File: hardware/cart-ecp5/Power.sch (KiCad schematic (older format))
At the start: 31 parts

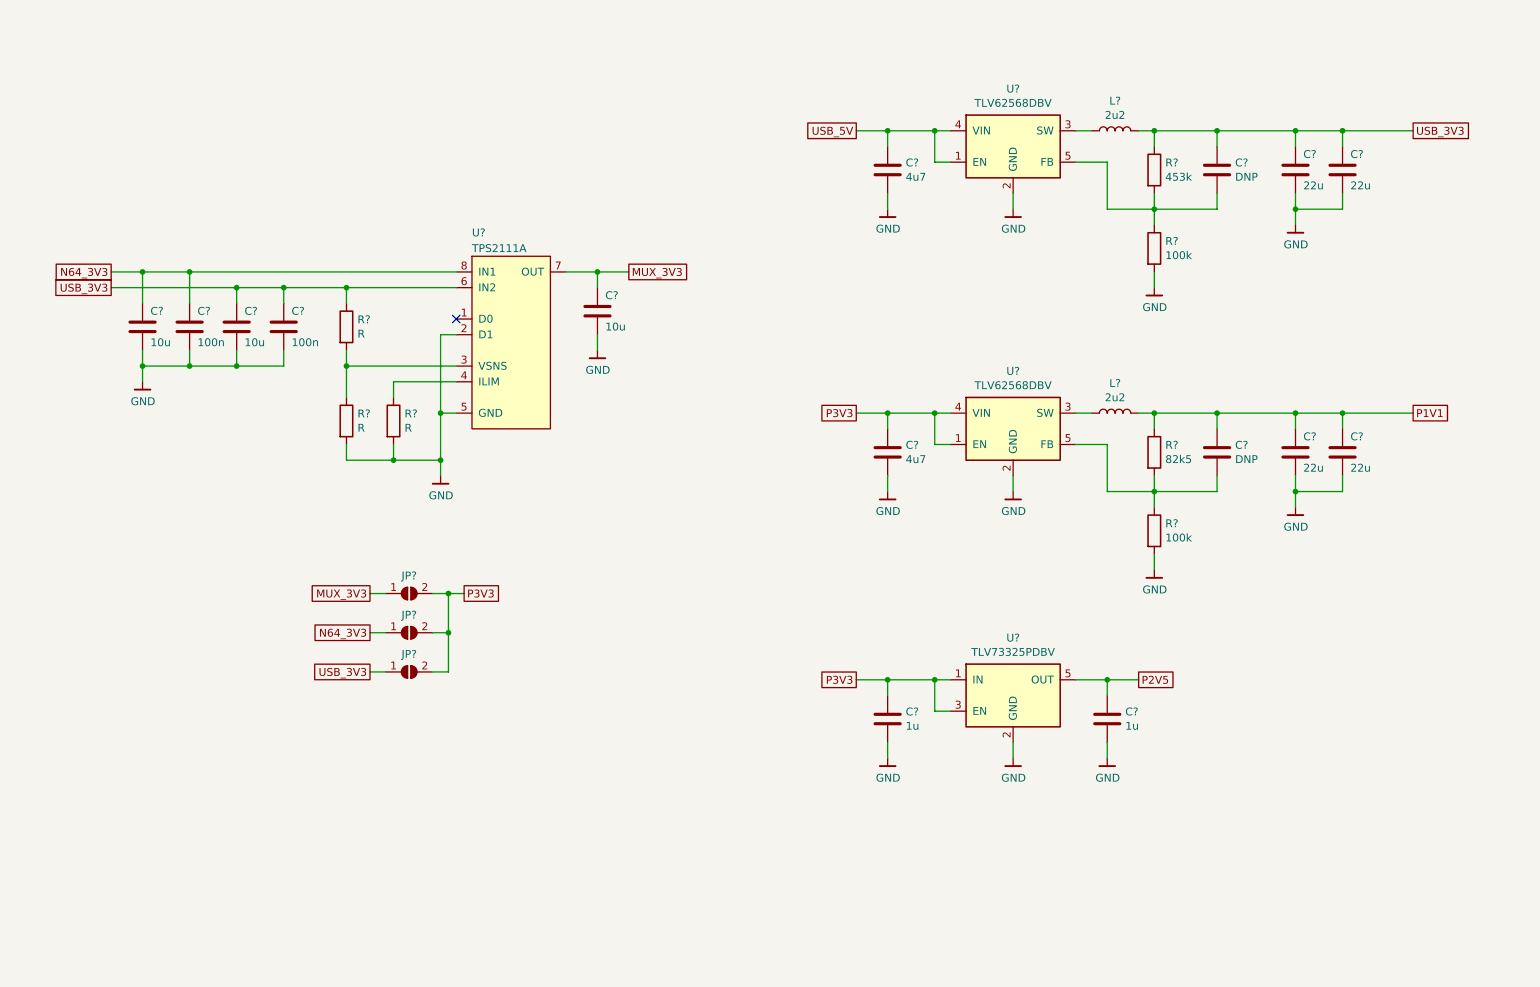
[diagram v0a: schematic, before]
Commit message: First pass annotation and footprint assignment complete
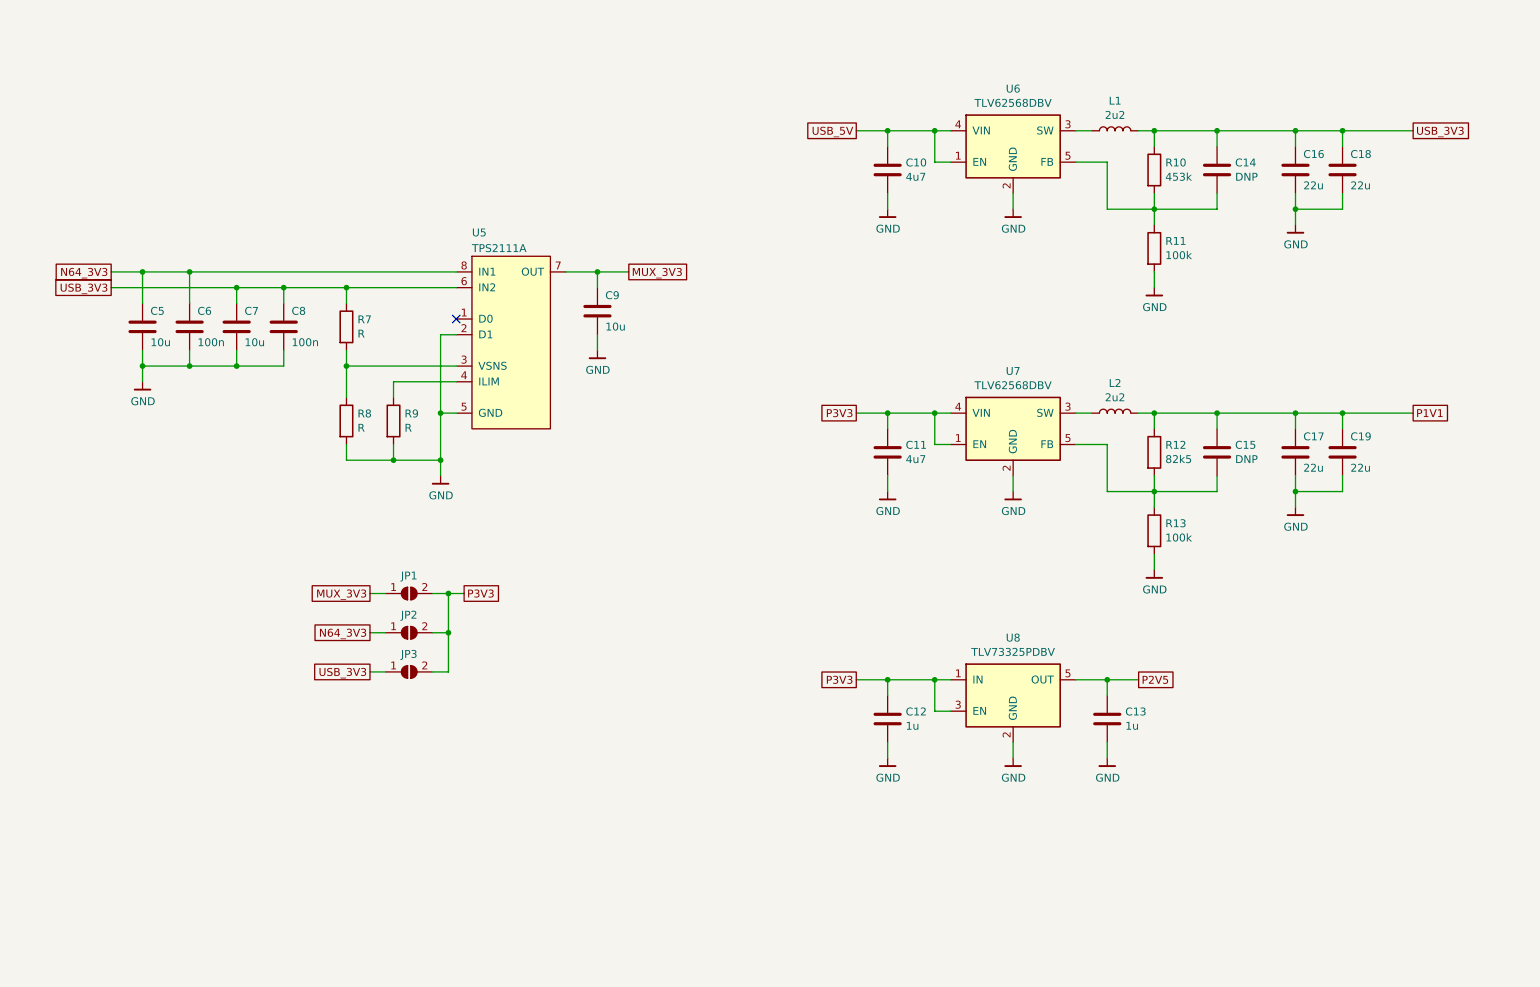
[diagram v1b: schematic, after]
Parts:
- C10, C11, C12, C13, C14, C15, C16, C17, C18, C19: renamed from C?; footprint (none) -> Capacitor_SMD:C_0603_1608Metric
- L1, L2: renamed from L?; footprint (none) -> Inductor_SMD:L_Taiyo-Yuden_NR-40xx
- R10, R11, R12, R13: renamed from R?; footprint (none) -> Resistor_SMD:R_0603_1608Metric
- gave numbers to parts that had none: 10

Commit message: Fixes for footprint assignment
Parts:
- C16, C17, C18, C19: footprint Capacitor_SMD:C_0603_1608Metric -> Capacitor_SMD:C_0805_2012Metric
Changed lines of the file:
@@
 F 0 "C18" H 9550 2150 50  0000 L CNN
 F 1 "22u" H 9550 1950 50  0000 L CNN
-F 2 "Capacitor_SMD:C_0603_1608Metric" H 9538 1900 50  0001 C CNN
+F 2 "Capacitor_SMD:C_0805_2012Metric" H 9538 1900 50  0001 C CNN
 F 3 "~" H 9500 2050 50  0001 C CNN
 	1    9500 2050
@@
 F 0 "C16" H 9250 2150 50  0000 L CNN
 F 1 "22u" H 9250 1950 50  0000 L CNN
-F 2 "Capacitor_SMD:C_0603_1608Metric" H 9238 1900 50  0001 C CNN
+F 2 "Capacitor_SMD:C_0805_2012Metric" H 9238 1900 50  0001 C CNN
 F 3 "~" H 9200 2050 50  0001 C CNN
 	1    9200 2050
@@
 F 0 "C19" H 9550 3950 50  0000 L CNN
 F 1 "22u" H 9550 3750 50  0000 L CNN
-F 2 "Capacitor_SMD:C_0603_1608Metric" H 9538 3700 50  0001 C CNN
+F 2 "Capacitor_SMD:C_0805_2012Metric" H 9538 3700 50  0001 C CNN
 F 3 "~" H 9500 3850 50  0001 C CNN
 	1    9500 3850
@@
 F 0 "C17" H 9250 3950 50  0000 L CNN
 F 1 "22u" H 9250 3750 50  0000 L CNN
-F 2 "Capacitor_SMD:C_0603_1608Metric" H 9238 3700 50  0001 C CNN
+F 2 "Capacitor_SMD:C_0805_2012Metric" H 9238 3700 50  0001 C CNN
 F 3 "~" H 9200 3850 50  0001 C CNN
 	1    9200 3850

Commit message: Assign FPGA pins for N64 cartridge bus
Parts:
- C14, C15, C52, C53: footprint Capacitor_SMD:C_0603_1608Metric -> Capacitor_SMD:C_0402_1005Metric
- C51: footprint Capacitor_SMD:C_0805_2012Metric -> Capacitor_SMD:C_0603_1608Metric
- R10, R11, R12, R13, R7, R8, R9: footprint Resistor_SMD:R_0603_1608Metric -> Resistor_SMD:R_0402_1005Metric
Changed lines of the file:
@@
 F 0 "R9" H 3520 3696 50  0000 L CNN
 F 1 "R" H 3520 3605 50  0000 L CNN
-F 2 "Resistor_SMD:R_0603_1608Metric" V 3380 3650 50  0001 C CNN
+F 2 "Resistor_SMD:R_0402_1005Metric" V 3380 3650 50  0001 C CNN
 F 3 "~" H 3450 3650 50  0001 C CNN
 	1    3450 3650
@@
 F 0 "R8" H 3220 3696 50  0000 L CNN
 F 1 "R" H 3220 3605 50  0000 L CNN
-F 2 "Resistor_SMD:R_0603_1608Metric" V 3080 3650 50  0001 C CNN
+F 2 "Resistor_SMD:R_0402_1005Metric" V 3080 3650 50  0001 C CNN
 F 3 "~" H 3150 3650 50  0001 C CNN
 	1    3150 3650
@@
 F 0 "R7" H 3220 3096 50  0000 L CNN
 F 1 "R" H 3220 3005 50  0000 L CNN
-F 2 "Resistor_SMD:R_0603_1608Metric" V 3080 3050 50  0001 C CNN
+F 2 "Resistor_SMD:R_0402_1005Metric" V 3080 3050 50  0001 C CNN
 F 3 "~" H 3150 3050 50  0001 C CNN
 	1    3150 3050
@@
 F 0 "C8" H 2800 3150 50  0000 L CNN
 F 1 "100n" H 2800 2950 50  0000 L CNN
-F 2 "Capacitor_SMD:C_0603_1608Metric" H 2788 2900 50  0001 C CNN
+F 2 "Capacitor_SMD:C_0402_1005Metric" H 2788 2900 50  0001 C CNN
 F 3 "~" H 2750 3050 50  0001 C CNN
 F 4 "" H 2750 3050 50  0001 C CNN "MPN"
@@
 F 0 "C6" H 2200 3150 50  0000 L CNN
 F 1 "100n" H 2200 2950 50  0000 L CNN
-F 2 "Capacitor_SMD:C_0603_1608Metric" H 2188 2900 50  0001 C CNN
+F 2 "Capacitor_SMD:C_0402_1005Metric" H 2188 2900 50  0001 C CNN
 F 3 "~" H 2150 3050 50  0001 C CNN
 F 4 "" H 2150 3050 50  0001 C CNN "MPN"
@@
 F 0 "C9" H 4800 3050 50  0000 L CNN
 F 1 "10u" H 4800 2850 50  0000 L CNN
-F 2 "Capacitor_SMD:C_0805_2012Metric" H 4788 2800 50  0001 C CNN
+F 2 "Capacitor_SMD:C_0603_1608Metric" H 4788 2800 50  0001 C CNN
 F 3 "~" H 4750 2950 50  0001 C CNN
 F 4 "" H 4750 2950 50  0001 C CNN "MPN"
@@
 F 0 "C14" H 8815 2096 50  0000 L CNN
 F 1 "DNP" H 8815 2005 50  0000 L CNN
-F 2 "Capacitor_SMD:C_0603_1608Metric" H 8738 1900 50  0001 C CNN
+F 2 "Capacitor_SMD:C_0402_1005Metric" H 8738 1900 50  0001 C CNN
 F 3 "~" H 8700 2050 50  0001 C CNN
 	1    8700 2050
@@
 F 0 "R10" H 8370 2096 50  0000 L CNN
 F 1 "453k" H 8370 2005 50  0000 L CNN
-F 2 "Resistor_SMD:R_0603_1608Metric" V 8230 2050 50  0001 C CNN
+F 2 "Resistor_SMD:R_0402_1005Metric" V 8230 2050 50  0001 C CNN
 F 3 "~" H 8300 2050 50  0001 C CNN
 	1    8300 2050
@@
 F 0 "R11" H 8370 2596 50  0000 L CNN
 F 1 "100k" H 8370 2505 50  0000 L CNN
-F 2 "Resistor_SMD:R_0603_1608Metric" V 8230 2550 50  0001 C CNN
+F 2 "Resistor_SMD:R_0402_1005Metric" V 8230 2550 50  0001 C CNN
 F 3 "~" H 8300 2550 50  0001 C CNN
 	1    8300 2550
@@
 F 0 "C15" H 8815 3896 50  0000 L CNN
 F 1 "DNP" H 8815 3805 50  0000 L CNN
-F 2 "Capacitor_SMD:C_0603_1608Metric" H 8738 3700 50  0001 C CNN
+F 2 "Capacitor_SMD:C_0402_1005Metric" H 8738 3700 50  0001 C CNN
 F 3 "~" H 8700 3850 50  0001 C CNN
 	1    8700 3850
@@
 F 0 "R12" H 8370 3896 50  0000 L CNN
 F 1 "82k5" H 8370 3805 50  0000 L CNN
-F 2 "Resistor_SMD:R_0603_1608Metric" V 8230 3850 50  0001 C CNN
+F 2 "Resistor_SMD:R_0402_1005Metric" V 8230 3850 50  0001 C CNN
 F 3 "~" H 8300 3850 50  0001 C CNN
 	1    8300 3850
@@
 F 0 "R13" H 8370 4396 50  0000 L CNN
 F 1 "100k" H 8370 4305 50  0000 L CNN
-F 2 "Resistor_SMD:R_0603_1608Metric" V 8230 4350 50  0001 C CNN
+F 2 "Resistor_SMD:R_0402_1005Metric" V 8230 4350 50  0001 C CNN
 F 3 "~" H 8300 4350 50  0001 C CNN
 	1    8300 4350

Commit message: Use 0805 power inductors
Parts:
- L1, L2: footprint Inductor_SMD:L_Taiyo-Yuden_NR-40xx -> Inductor_SMD:L_0805_2012Metric
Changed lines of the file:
@@
 F 0 "L1" V 8240 1800 50  0000 C CNN
 F 1 "2u2" V 8149 1800 50  0000 C CNN
-F 2 "Inductor_SMD:L_Taiyo-Yuden_NR-40xx" H 8050 1800 50  0001 C CNN
+F 2 "Inductor_SMD:L_0805_2012Metric" H 8050 1800 50  0001 C CNN
 F 3 "~" H 8050 1800 50  0001 C CNN
 	1    8050 1800
@@
 F 0 "L2" V 8240 3600 50  0000 C CNN
 F 1 "2u2" V 8149 3600 50  0000 C CNN
-F 2 "Inductor_SMD:L_Taiyo-Yuden_NR-40xx" H 8050 3600 50  0001 C CNN
+F 2 "Inductor_SMD:L_0805_2012Metric" H 8050 3600 50  0001 C CNN
 F 3 "~" H 8050 3600 50  0001 C CNN
 	1    8050 3600

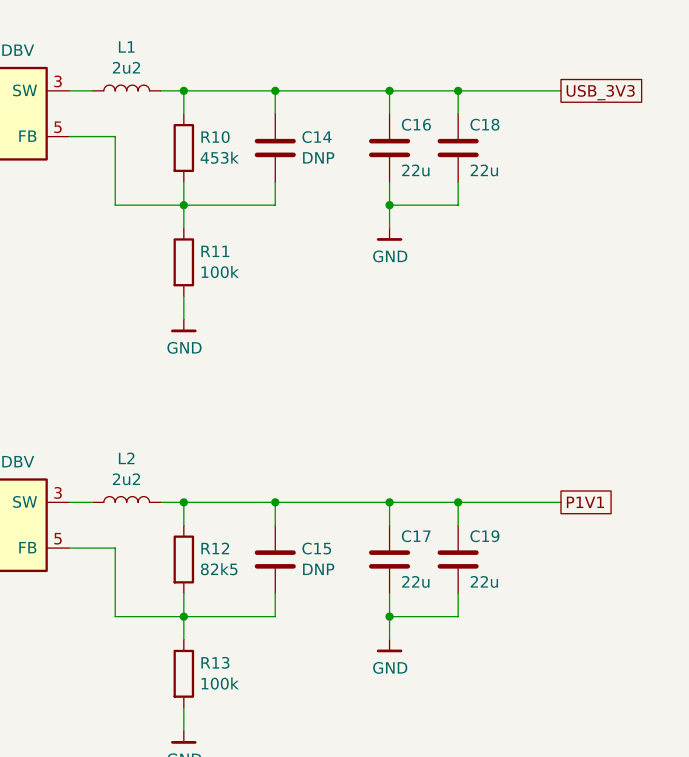
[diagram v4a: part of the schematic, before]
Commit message: Reduce the area of the voltage regulators
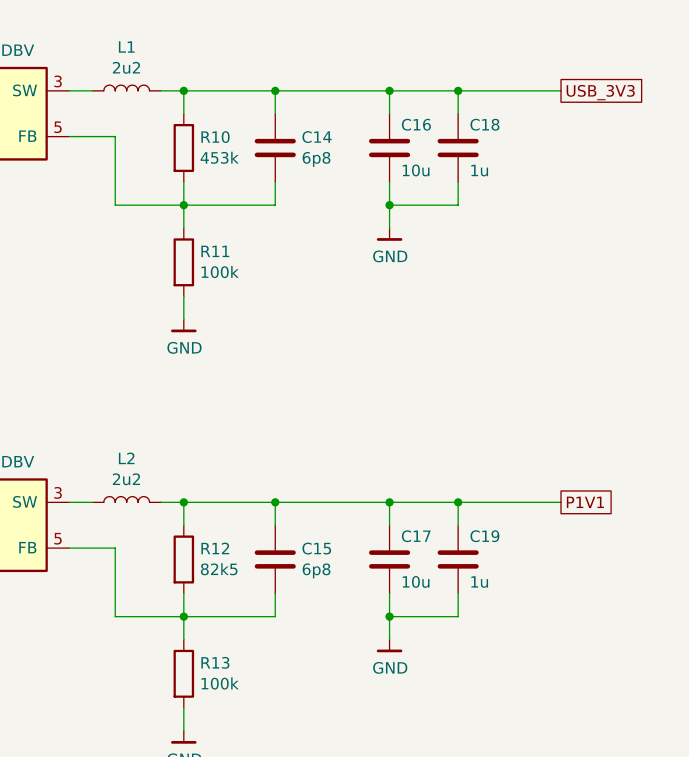
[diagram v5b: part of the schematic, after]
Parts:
- C10, C11, C12, C13: footprint Capacitor_SMD:C_0603_1608Metric -> Capacitor_SMD:C_0402_1005Metric
- C14, C15: value DNP -> 6p8
- C16, C17: value 22u -> 10u; footprint Capacitor_SMD:C_0805_2012Metric -> Capacitor_SMD:C_0603_1608Metric
- C18, C19: value 22u -> 1u; footprint Capacitor_SMD:C_0805_2012Metric -> Capacitor_SMD:C_0402_1005Metric
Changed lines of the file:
@@
 P 9500 2050
 F 0 "C18" H 9550 2150 50  0000 L CNN
-F 1 "22u" H 9550 1950 50  0000 L CNN
-F 2 "Capacitor_SMD:C_0805_2012Metric" H 9538 1900 50  0001 C CNN
+F 1 "1u" H 9550 1950 50  0000 L CNN
+F 2 "Capacitor_SMD:C_0402_1005Metric" H 9538 1900 50  0001 C CNN
 F 3 "~" H 9500 2050 50  0001 C CNN
 	1    9500 2050
@@
 P 8700 2050
 F 0 "C14" H 8815 2096 50  0000 L CNN
-F 1 "DNP" H 8815 2005 50  0000 L CNN
+F 1 "6p8" H 8815 2005 50  0000 L CNN
 F 2 "Capacitor_SMD:C_0402_1005Metric" H 8738 1900 50  0001 C CNN
 F 3 "~" H 8700 2050 50  0001 C CNN
@@
 F 0 "C10" H 6715 2096 50  0000 L CNN
 F 1 "4u7" H 6715 2005 50  0000 L CNN
-F 2 "Capacitor_SMD:C_0603_1608Metric" H 6638 1900 50  0001 C CNN
+F 2 "Capacitor_SMD:C_0402_1005Metric" H 6638 1900 50  0001 C CNN
 F 3 "~" H 6600 2050 50  0001 C CNN
 	1    6600 2050
@@
 P 9200 2050
 F 0 "C16" H 9250 2150 50  0000 L CNN
-F 1 "22u" H 9250 1950 50  0000 L CNN
-F 2 "Capacitor_SMD:C_0805_2012Metric" H 9238 1900 50  0001 C CNN
+F 1 "10u" H 9250 1950 50  0000 L CNN
+F 2 "Capacitor_SMD:C_0603_1608Metric" H 9238 1900 50  0001 C CNN
 F 3 "~" H 9200 2050 50  0001 C CNN
 	1    9200 2050
@@
 P 9500 3850
 F 0 "C19" H 9550 3950 50  0000 L CNN
-F 1 "22u" H 9550 3750 50  0000 L CNN
-F 2 "Capacitor_SMD:C_0805_2012Metric" H 9538 3700 50  0001 C CNN
+F 1 "1u" H 9550 3750 50  0000 L CNN
+F 2 "Capacitor_SMD:C_0402_1005Metric" H 9538 3700 50  0001 C CNN
 F 3 "~" H 9500 3850 50  0001 C CNN
 	1    9500 3850
@@
 P 8700 3850
 F 0 "C15" H 8815 3896 50  0000 L CNN
-F 1 "DNP" H 8815 3805 50  0000 L CNN
+F 1 "6p8" H 8815 3805 50  0000 L CNN
 F 2 "Capacitor_SMD:C_0402_1005Metric" H 8738 3700 50  0001 C CNN
 F 3 "~" H 8700 3850 50  0001 C CNN
@@
 F 0 "C11" H 6715 3896 50  0000 L CNN
 F 1 "4u7" H 6715 3805 50  0000 L CNN
-F 2 "Capacitor_SMD:C_0603_1608Metric" H 6638 3700 50  0001 C CNN
+F 2 "Capacitor_SMD:C_0402_1005Metric" H 6638 3700 50  0001 C CNN
 F 3 "~" H 6600 3850 50  0001 C CNN
 	1    6600 3850
@@
 P 9200 3850
 F 0 "C17" H 9250 3950 50  0000 L CNN
-F 1 "22u" H 9250 3750 50  0000 L CNN
-F 2 "Capacitor_SMD:C_0805_2012Metric" H 9238 3700 50  0001 C CNN
+F 1 "10u" H 9250 3750 50  0000 L CNN
+F 2 "Capacitor_SMD:C_0603_1608Metric" H 9238 3700 50  0001 C CNN
 F 3 "~" H 9200 3850 50  0001 C CNN
 	1    9200 3850
@@
 F 0 "C12" H 6715 5596 50  0000 L CNN
 F 1 "1u" H 6715 5505 50  0000 L CNN
-F 2 "Capacitor_SMD:C_0603_1608Metric" H 6638 5400 50  0001 C CNN
+F 2 "Capacitor_SMD:C_0402_1005Metric" H 6638 5400 50  0001 C CNN
 F 3 "~" H 6600 5550 50  0001 C CNN
 	1    6600 5550
@@
 F 0 "C13" H 8115 5596 50  0000 L CNN
 F 1 "1u" H 8115 5505 50  0000 L CNN
-F 2 "Capacitor_SMD:C_0603_1608Metric" H 8038 5400 50  0001 C CNN
+F 2 "Capacitor_SMD:C_0402_1005Metric" H 8038 5400 50  0001 C CNN
 F 3 "~" H 8000 5550 50  0001 C CNN
 	1    8000 5550

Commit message: Reduce area of the power mux
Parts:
- C3, C4: footprint Capacitor_SMD:C_0805_2012Metric -> Capacitor_SMD:C_0603_1608Metric
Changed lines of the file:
@@
 F 0 "C7" H 2500 3150 50  0000 L CNN
 F 1 "10u" H 2500 2950 50  0000 L CNN
-F 2 "Capacitor_SMD:C_0805_2012Metric" H 2488 2900 50  0001 C CNN
+F 2 "Capacitor_SMD:C_0603_1608Metric" H 2488 2900 50  0001 C CNN
 F 3 "~" H 2450 3050 50  0001 C CNN
 F 4 "" H 2450 3050 50  0001 C CNN "MPN"
@@
 F 0 "C5" H 1900 3150 50  0000 L CNN
 F 1 "10u" H 1900 2950 50  0000 L CNN
-F 2 "Capacitor_SMD:C_0805_2012Metric" H 1888 2900 50  0001 C CNN
+F 2 "Capacitor_SMD:C_0603_1608Metric" H 1888 2900 50  0001 C CNN
 F 3 "~" H 1850 3050 50  0001 C CNN
 F 4 "" H 1850 3050 50  0001 C CNN "MPN"
